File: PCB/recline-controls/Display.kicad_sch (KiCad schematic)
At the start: 0 parts

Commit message: Recline Controls
Recline Control board and human machine interface board schematic complete !
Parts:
- added J5: PPTC101LFBN-RC, AVR-KiCAD-Lib-Connectors:Female_Header_Straight_1x10_Pitch2.54mm, symbol AVR-KiCAD-Lib-Connectors:PPTC101LFBN-RC
- added R22, R23, R24, R25, R26, R27, R28, R29: RC0402FR-07220RL, AVR-KiCAD-Lib-Resistors:R0402, symbol AVR-KiCAD-Lib-Resistors:RC0402FR-07220RL
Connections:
- new net: J5.9, R28.2
- new net: J5.10, R29.2
- new net: J5.1, R22.2
- new net: J5.2, R23.2
- new net: J5.3, R24.2
- new net: J5.4, R25.2
- new net: J5.7, R26.2
- new net: J5.8, R27.2
- new net 7SEG0: R22.1
- new net 7SEG1: R23.1
- new net 7SEG2: R24.1
- new net 7SEG3: R25.1
- new net 7SEG4: R26.1
- new net 7SEG5: R27.1
- new net 7SEG6: R28.1
- new net 7SEG7: R29.1
- new net GND: J5.5, J5.6

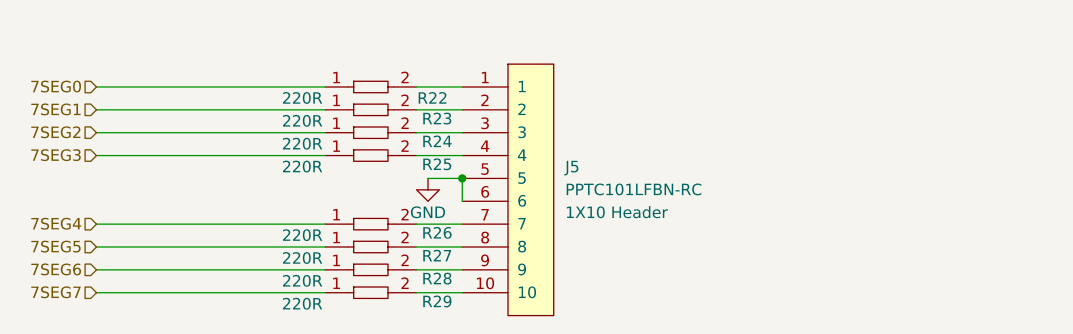
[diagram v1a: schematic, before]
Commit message: PCB Started
PCB design for Recline Control Board started, figuring out PCB shape and connector positioning, work in progress !
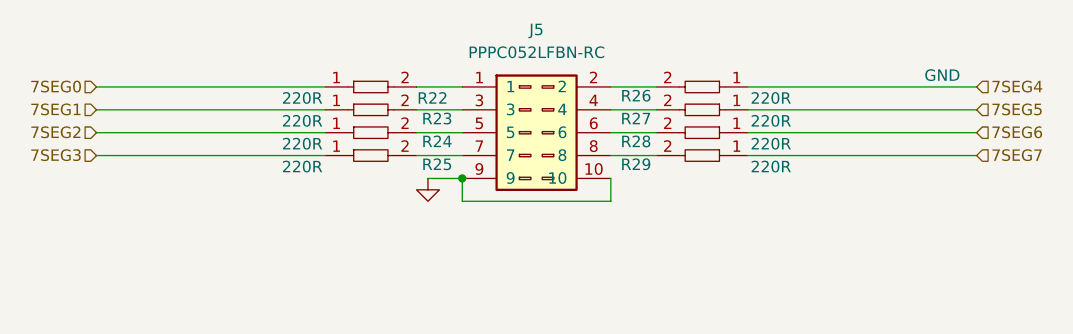
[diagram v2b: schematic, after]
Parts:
- removed J5: PPTC101LFBN-RC, AVR-KiCAD-Lib-Connectors:Female_Header_Straight_1x10_Pitch2.54mm, symbol AVR-KiCAD-Lib-Connectors:PPTC101LFBN-RC
- added J5: PPPC052LFBN-RC, AVR-KiCAD-Lib-Connectors:PPPC052LFBN-RC_2x05_Pitch2.54mm, symbol AVR-KiCAD-Lib-Connectors:PPPC052LFBN-RC
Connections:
- net GND: now also J5.10, J5.9
- net at R28.2: now also J5.6
- net at R29.2: now also J5.8
- net at R22.2: now also J5.1
- net at R23.2: now also J5.3
- net at R24.2: now also J5.5
- net at R25.2: now also J5.7
- net at R26.2: now also J5.2
- net at R27.2: now also J5.4
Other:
- moved on the sheet: R26, R27, R28, R29

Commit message: All Hardware Tweaked / 3D Renders
PCBs for Actuator Control, Recline Control HID, and 7 Segment carrier are all complete with full 3D models rendering. 3D Renders of all board added to repository img directory.
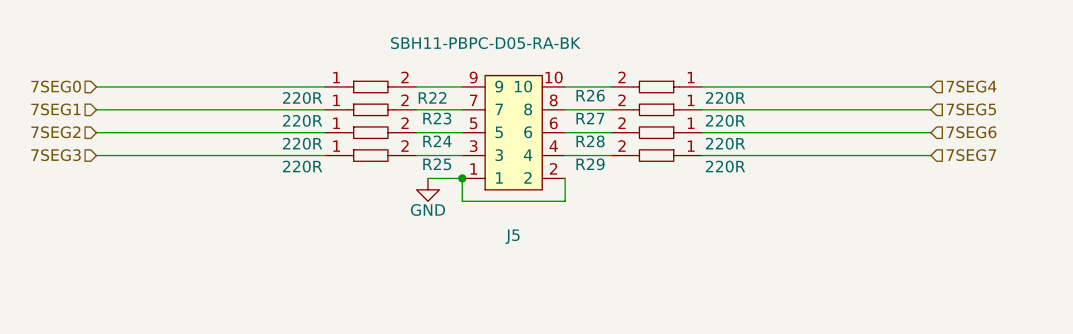
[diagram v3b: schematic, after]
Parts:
- removed J5: PPPC052LFBN-RC, AVR-KiCAD-Lib-Connectors:PPPC052LFBN-RC_2x05_Pitch2.54mm, symbol AVR-KiCAD-Lib-Connectors:PPPC052LFBN-RC
- added J5: SBH11-PBPC-D05-RA-BK, AVR-KiCAD-Lib-Connectors:CONN10_D05-RA-BK_SUL, symbol AVR-KiCAD-Lib-Connectors:SBH11-PBPC-D05-RA-BK
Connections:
- net GND: now also J5.1, J5.2
- net at R28.2: now also J5.6
- net at R29.2: now also J5.4
- net at R22.2: now also J5.9
- net at R23.2: now also J5.7
- net at R27.2: now also J5.8
- net at R26.2: now also J5.10
- net at R24.2: now also J5.5
- net at R25.2: now also J5.3
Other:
- moved on the sheet: R26, R27, R28, R29
